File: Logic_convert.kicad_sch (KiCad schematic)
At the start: 25 parts, among them U10 LM324A, U11 LM324A, U12 CD4504B, U13 CD4504B, U14 CD4504B

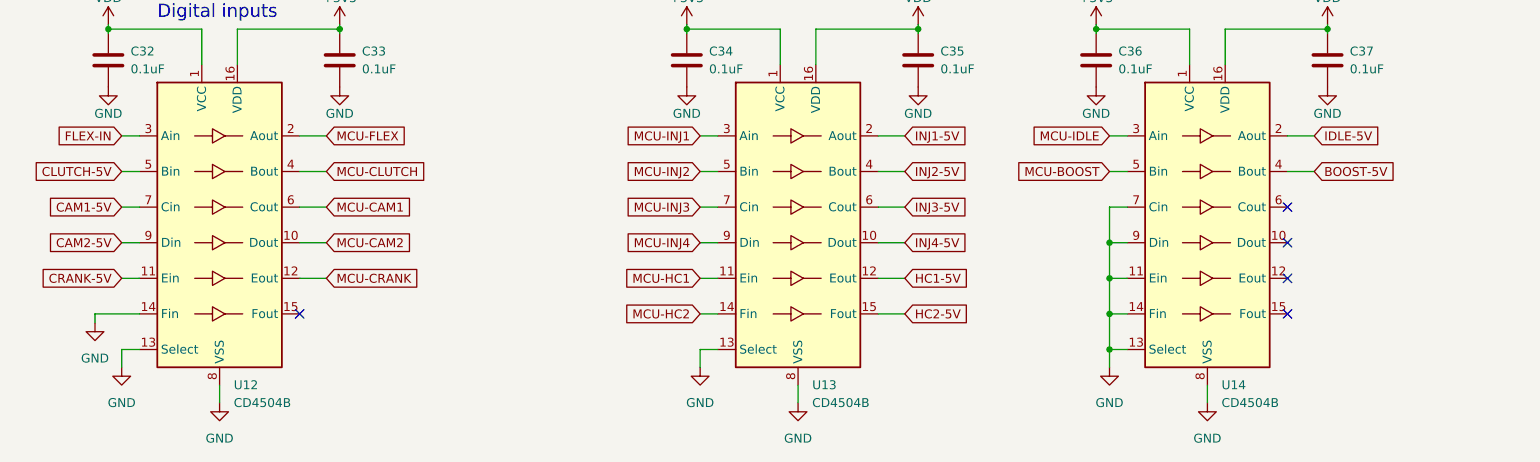
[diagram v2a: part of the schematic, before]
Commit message: Completed layout, slight changes to schematic to optimise routing, 12V proto supply rail removed
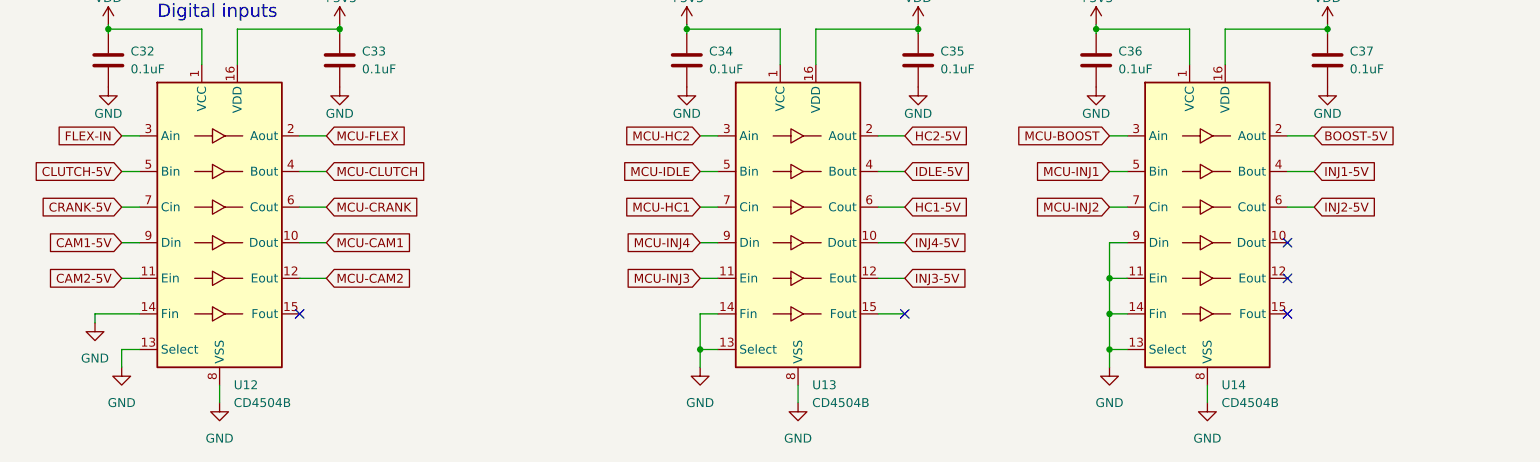
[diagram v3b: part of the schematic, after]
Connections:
- net BOOST-5V: now also U14.2 (Aout); no longer U14.4 (Bout)
- net CAM1-5V: now also U12.9 (Din); no longer U12.7 (Cin)
- net CAM2-5V: now also U12.11 (Ein); no longer U12.9 (Din)
- net CRANK-5V: now also U12.7 (Cin); no longer U12.11 (Ein)
- net GND: now also U13.14 (Fin); no longer U14.7 (Cin)
- net HC1-5V: now also U13.6 (Cout); no longer U13.12 (Eout)
- net HC2-5V: now also U13.2 (Aout); no longer U13.15 (Fout)
- net IDLE-5V: now also U13.4 (Bout); no longer U14.2 (Aout)
- net INJ1-5V: now also U14.4 (Bout); no longer U13.2 (Aout)
- net INJ2-5V: now also U14.6 (Cout); no longer U13.4 (Bout)
- net INJ3-5V: now also U13.12 (Eout); no longer U13.6 (Cout)
- net MCU-BOOST: now also U14.3 (Ain); no longer U14.5 (Bin)
- net MCU-CAM1: now also U12.10 (Dout); no longer U12.6 (Cout)
- net MCU-CAM2: now also U12.12 (Eout); no longer U12.10 (Dout)
- net MCU-CRANK: now also U12.6 (Cout); no longer U12.12 (Eout)
- net MCU-HC1: now also U13.7 (Cin); no longer U13.11 (Ein)
- net MCU-HC2: now also U13.3 (Ain); no longer U13.14 (Fin)
- net MCU-IDLE: now also U13.5 (Bin); no longer U14.3 (Ain)
- net MCU-INJ1: now also U14.5 (Bin); no longer U13.3 (Ain)
- net MCU-INJ2: now also U14.7 (Cin); no longer U13.5 (Bin)
- net MCU-INJ3: now also U13.11 (Ein); no longer U13.7 (Cin)
